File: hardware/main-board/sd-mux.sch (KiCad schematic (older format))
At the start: 91 parts, among them J1 USDCARD, P1 USB_OTG, P10 BARREL_JACK, P2 61400416021, P3 61400416021, P4 CONN_01X06, P5 BARREL_JACK, P6 IDC_02X04, P7 IDC_02X04, P8 USB_OTG, P9 USB_A, Q1 IRF7606PBF, Q2 IRF7606PBF, Q3 IRF7606PBF, Q4 IRF7606PBF, Q5 2N7002, Q6 2N7002, Q7 IRF7606PBF, Q8 IRF7606PBF, U1 TS3USB30EDGSR, U2 FT245RL, U3 TUSB4041IPAPR, U4 74AHC1G14, U5 TLV73333, U6 TLV73311, U7 74AHC1G14, U8 TS3A27518E, Y1 24MHz

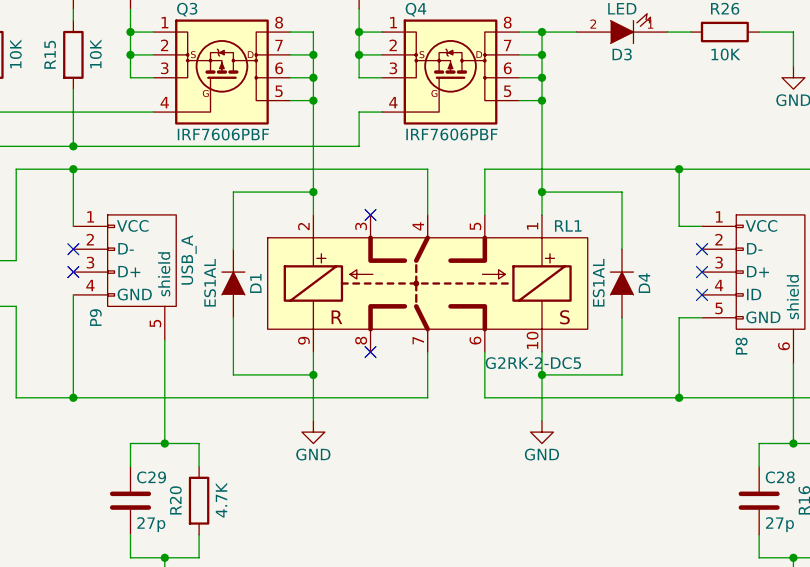
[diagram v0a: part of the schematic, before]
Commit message: Update BOM and layout labels
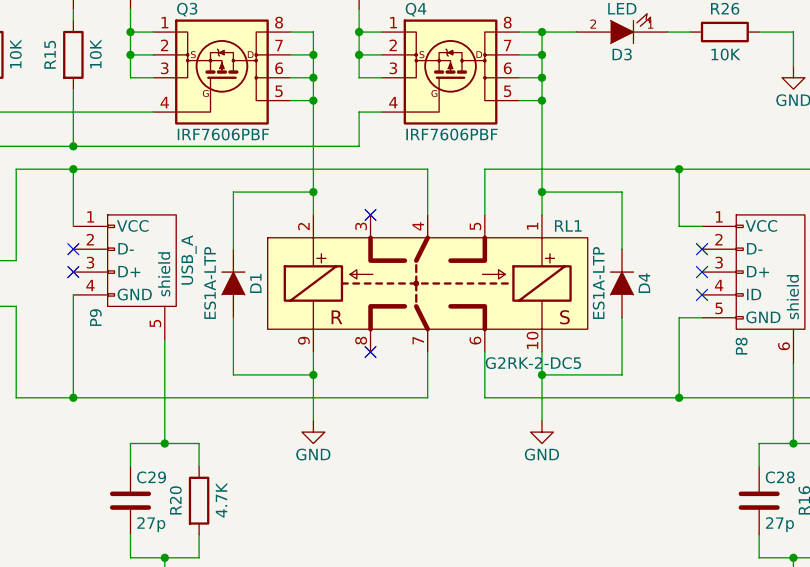
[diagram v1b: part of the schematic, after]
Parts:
- D1, D4: value ES1AL -> ES1A-LTP; footprint footprints:do219ab -> Diodes_SMD:SMA_Handsoldering
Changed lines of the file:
@@
 P 19550 12850
 F 0 "D4" H 19550 12950 50  0000 C CNN
-F 1 "ES1AL" H 19550 12750 50  0000 C CNN
-F 2 "footprints:do219ab" H 19550 12850 60  0001 C CNN
-F 3 "http://www.farnell.com/datasheets/1706585.pdf" H 19550 12850 60  0001 C CNN
+F 1 "ES1A-LTP" H 19550 12750 50  0000 C CNN
+F 2 "Diodes_SMD:SMA_Handsoldering" H 19550 12850 60  0001 C CNN
+F 3 "" H 19550 12850 60  0001 C CNN
 	1    19550 12850
 	0    1    1    0
@@
 P 17850 12850
 F 0 "D1" H 17850 12950 50  0000 C CNN
-F 1 "ES1AL" H 17850 12750 50  0000 C CNN
-F 2 "footprints:do219ab" H 17850 12850 60  0001 C CNN
-F 3 "http://www.farnell.com/datasheets/1706585.pdf" H 17850 12850 60  0001 C CNN
+F 1 "ES1A-LTP" H 17850 12750 50  0000 C CNN
+F 2 "Diodes_SMD:SMA_Handsoldering" H 17850 12850 60  0001 C CNN
+F 3 "" H 17850 12850 60  0001 C CNN
 	1    17850 12850
 	0    1    1    0
